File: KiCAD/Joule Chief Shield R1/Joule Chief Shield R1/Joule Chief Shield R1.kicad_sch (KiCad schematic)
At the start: 98 parts, among them J1 Power, J12 Conn_01x06, J13 Conn_01x06, J14 Conn_01x06, J15 Conn_01x06, J16 Conn_01x06, J17 Conn_01x06, J18 Conn_01x06, J2 Digital/PWM, J3 Analog, J4 Digital/PWM, Q10 AO3400A, Q11 AO3400A, Q12 AO3400A, Q3 AO3400A, Q4 AO3400A, Q5 AO3400A, Q6 AO3400A, Q7 AO3400A, Q8 AO3400A, Q9 AO3400A, U11 INA219AxD, U7 LTC3105xMS, U8 AD5280, U9 INA219AxD

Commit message: both schematics finished
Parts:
- removed LITH2: 18650, Joule Thief-Library:18650_Cell_Clip, symbol Device:Battery_Cell
- removed Q3: AO3400A, Package_TO_SOT_SMD:SOT-23, symbol Transistor_FET:AO3400A
- removed R27, R29, R31, R33, R35, R37, R39, R41: 500, Resistor_SMD:R_0805_2012Metric_Pad1.20x1.40mm_HandSolder, symbol Device:R_Small
- removed U10: ~, symbol Joule_Thief_R1:BMS_BOARD
- added C12, C13: 0.1u, Capacitor_SMD:C_0805_2012Metric_Pad1.18x1.45mm_HandSolder, symbol Device:C_Small
- added C14: 10u, Capacitor_SMD:C_0805_2012Metric_Pad1.18x1.45mm_HandSolder, symbol Device:C_Small
- added D1, D2: LED, symbol Device:LED
- added LITH1: 18650, Joule Thief-Library:18650_Cell_Clip, symbol Device:Battery_Cell
- added Q1: AO3400A, Package_TO_SOT_SMD:SOT-23, symbol Transistor_FET:AO3400A
- added R10, R11, R12, R13: 1k, Resistor_SMD:R_0805_2012Metric_Pad1.20x1.40mm_HandSolder, symbol Device:R_Small
- added R14: 10k, Resistor_SMD:R_0805_2012Metric_Pad1.20x1.40mm_HandSolder, symbol Device:R_Small
- added R18, R20, R21, R22, R23, R24, R25: 1K, Resistor_SMD:R_0805_2012Metric_Pad1.20x1.40mm_HandSolder, symbol Device:R_Small
- added R9: 100, Resistor_SMD:R_0805_2012Metric_Pad1.20x1.40mm_HandSolder, symbol Device:R_Small
- added U5: DW01, Package_TO_SOT_SMD:SOT-23-6_Handsoldering, symbol 000_Dropbin:DW01
- added U6: TP4056, Package_SO:SOIC-8-1EP_3.9x4.9mm_P1.27mm_EP2.29x3mm, symbol 000_Dropbin:TP4056
- added U7: FS8205A, Package_TO_SOT_SMD:SOT-23-6_Handsoldering, symbol 000_Dropbin:FS8205A
- R17: renamed from R26; value 500 -> 1K
- R19: value 10k -> 1K
- renumbered C21 to C1, C19 to C10, C18 to C11, C22 to C2, C23 to C3, C17 to C4, C20 to C5, C13 to C6, C14 to C7, C16 to C8, C15 to C9, D8 to D10, D9 to D11, D1 to D3, D2 to D4, D3 to D5, D4 to D6, D5 to D7, D6 to D8, D7 to D9, J12 to J1, J3 to J10, J4 to J11, J13 to J2, J14 to J3, J15 to J4, J16 to J5, J17 to J6, J18 to J7, J2 to J8, J1 to J9, JP41 to JP1, JP30 to JP10, JP31 to JP11, JP32 to JP12, JP40 to JP13, JP39 to JP14, JP38 to JP15, JP37 to JP16, JP36 to JP17, JP35 to JP18, JP34 to JP19, JP42 to JP2, JP33 to JP20, JP43 to JP3, JP44 to JP4, JP45 to JP5, JP46 to JP6, JP47 to JP7, JP48 to JP8, JP29 to JP9, L2 to L1, Q12 to Q10, Q4 to Q2, Q5 to Q3, Q6 to Q4, Q7 to Q5, Q8 to Q6, Q9 to Q7, Q10 to Q8, Q11 to Q9, R21 to R1, R23 to R15, R24 to R16, R20 to R2, R25 to R26, R28 to R27, R30 to R28, R32 to R29, R22 to R3, R34 to R30, R36 to R31, R38 to R32, R40 to R33, R42 to R34, R14 to R4, R15 to R5, R17 to R6, R18 to R7, R16 to R8, U11 to U1, U7 to U2, U8 to U3, U9 to U4
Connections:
- net +5V: now also R19.2, R18.2, R20.2, R21.2, R22.2, R23.2, R24.2, R25.2
- net CHARGER: now also Q1.1 (G), R14.2; no longer R19.2
- net GND: now also Q1.2 (S), R14.1; no longer R19.1
- net at D11.2 (A): now also R25.1
- net at D9.2 (A): now also R23.1
- net at D4.2 (A): now also R18.1
- net at D5.2 (A): now also R19.1
- net at R6.1: now also C13.2, D1.2 (A), D2.2 (A), U6.4 (VCC), U6.8 (CE)
- net at D7.2 (A): now also R21.1
- net at D6.2 (A): now also R20.1
- net at D10.2 (A): now also R24.1
- net at D8.2 (A): now also R22.1
- new net: C13.1, C14.1, Q1.3 (D), R12.1, R13.1, U6.1 (TEMP), U6.3 (GND), U7.6 (S2), U7.7 (S2)
- new net: C12.2, C14.2, R9.1, U5.5 (VCC), U6.5 (BAT)
- new net: U5.1 (OD), U7.4 (G1)
- new net: R12.2, U5.2 (CS)
- new net: U5.3 (OC), U7.5 (G2)
- new net: R13.2, U6.2 (PROG)
- new net: D2.1 (K), R11.1
- new net: D1.1 (K), R10.1
- new net: R10.2, U6.7 (~{CHRG})
- new net: R11.2, U6.6 (~{STDBY})
- new net BAT+: LITH1.1 (+), R9.2
- new net BAT-: C12.1, LITH1.2 (-), U5.6 (GND), U7.2 (S1), U7.3 (S1)
- no-connect marks 5 -> 8
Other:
- note added: "18650 BMS+CHARGING MODULE"
- note removed: "GENERIC BMS MODULE"
- moved on the sheet: C1, C10, C11, C2, C3, C4, C5, C6, C7, C8, C9, D10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

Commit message: ERC+prep for board layout
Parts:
- C2, C5: footprint (none) -> 000_Dropbin:1F_Supercap
- C4: footprint (none) -> Capacitor_THT:CP_Radial_D5.0mm_P2.00mm
- D1, D10, D11, D2, D3, D4, D5, D6, D7, D8, D9: footprint (none) -> LED_SMD:LED_0805_2012Metric_Pad1.15x1.40mm_HandSolder
- J1, J2, J3, J4, J5, J6, J7: footprint (none) -> Connector_JST:JST_PH_B7B-PH-K_1x07_P2.00mm_Vertical
- JP1, JP10, JP11, JP12, JP13, JP14, JP15, JP16, JP17, JP18, JP19, JP2, JP20, JP3, JP4, JP5, JP6, JP7, JP8, JP9: footprint (none) -> Jumper:SolderJumper-2_P1.3mm_Open_RoundedPad1.0x1.5mm
- L1: footprint Joule Thief-Library:Power_Inductor_101040 -> 000_Dropbin:Power_Inductor_101040
- LITH1: footprint Joule Thief-Library:18650_Cell_Clip -> 000_Dropbin:18650_Cell_Clip_V2
- TPx1: footprint (none) -> TestPoint:TestPoint_THTPad_1.0x1.0mm_Drill0.5mm
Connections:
- no-connect marks 8 -> 23
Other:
- note added: "INCOMING POWER MONITOR"
- note added: "OUTGOING POWER MONITOR"
- note removed: "LOAD CELL POWER MONITOR"
- note removed: "SUPPLY CELL POWER MONITOR"

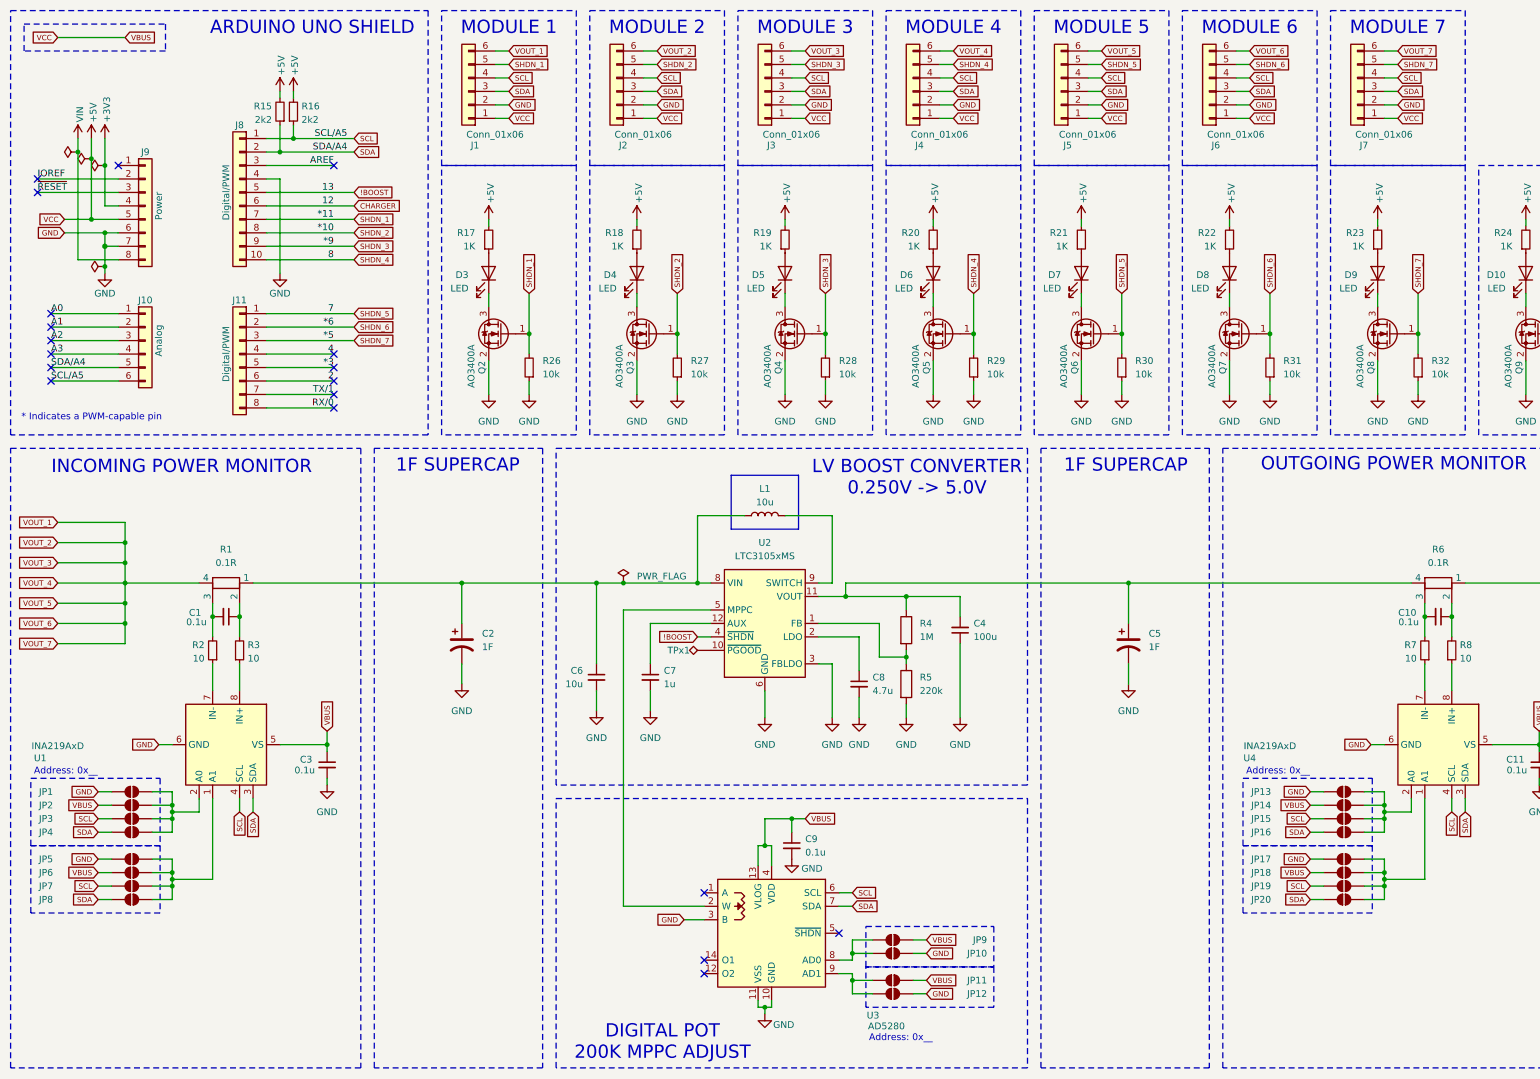
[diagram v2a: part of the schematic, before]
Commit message: layout extraction module
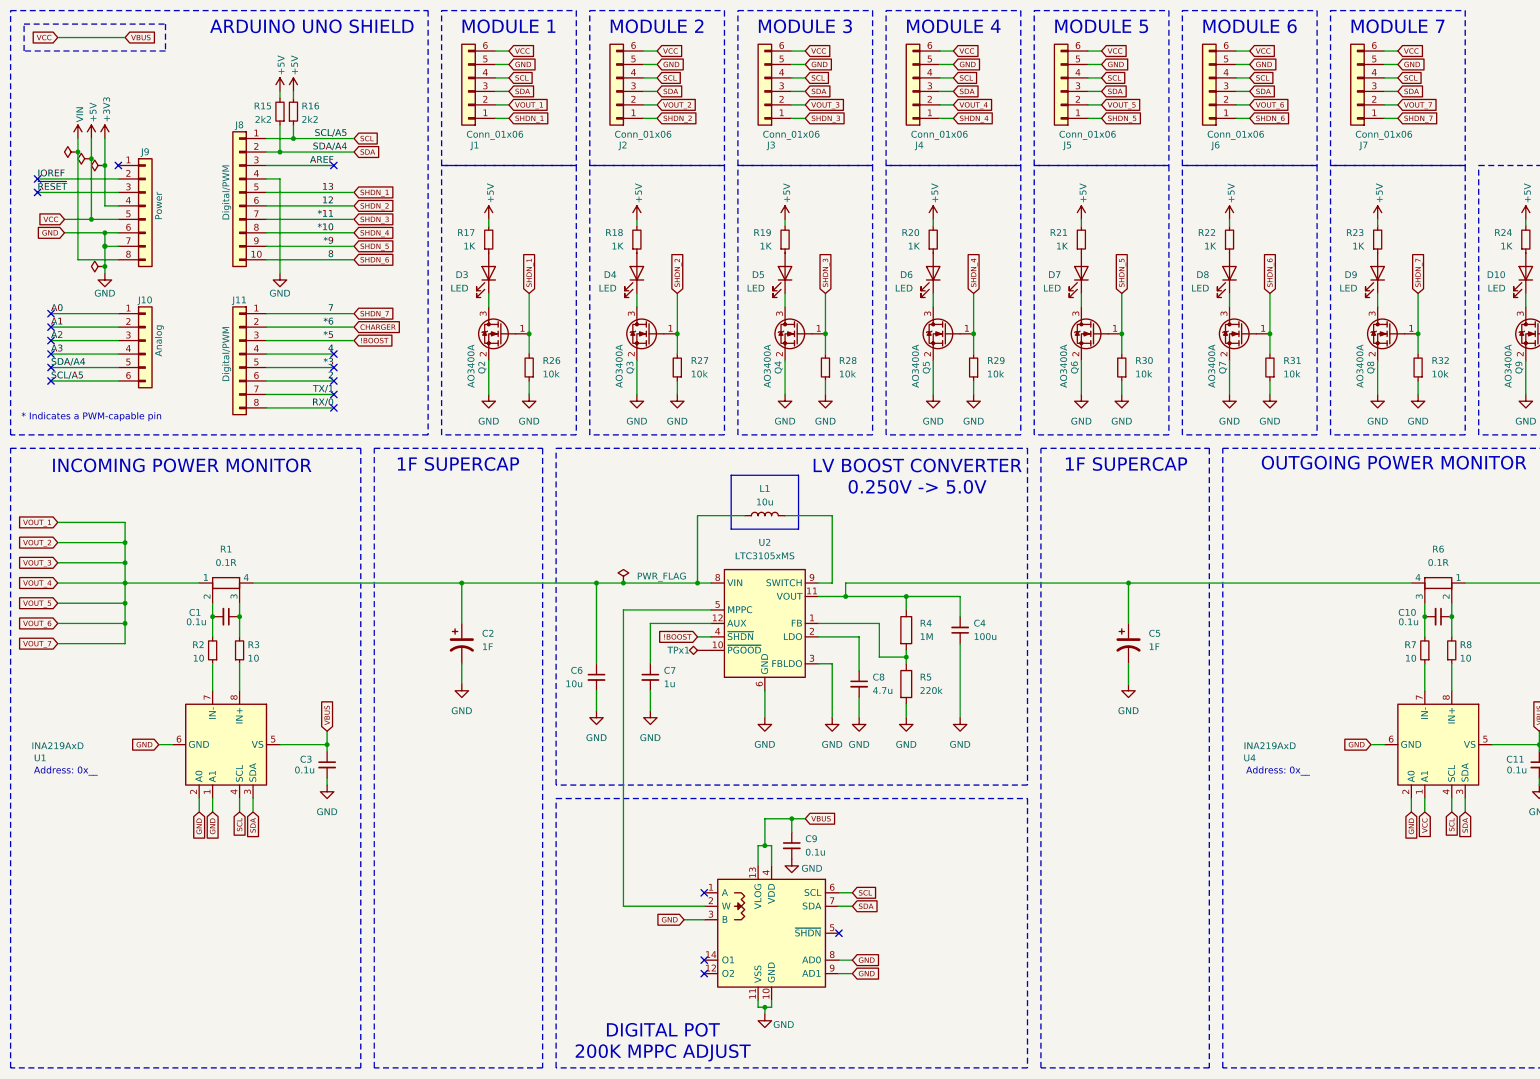
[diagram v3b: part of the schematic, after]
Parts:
- removed JP1, JP10, JP11, JP12, JP13, JP14, JP15, JP16, JP17, JP18, JP19, JP2, JP20, JP3, JP4, JP5, JP6, JP7, JP8, JP9: SolderJumper_2_Open, Jumper:SolderJumper-2_P1.3mm_Open_RoundedPad1.0x1.5mm, symbol Jumper:SolderJumper_2_Open
- J1, J2, J3, J4, J5, J6, J7: footprint Connector_JST:JST_PH_B7B-PH-K_1x07_P2.00mm_Vertical -> Connector_JST:JST_PH_B6B-PH-K_1x06_P2.00mm_Vertical
- R1, R6: footprint Resistor_SMD:R_Shunt_Vishay_WSK2512_6332Metric_T1.19mm -> 000_Dropbin:R_Shunt_2512_V2
- U7: footprint Package_TO_SOT_SMD:SOT-23-6_Handsoldering -> Package_TO_SOT_SMD:SOT-23-8_Handsoldering
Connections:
- net !BOOST: now also J11.3 (Pin_3); no longer J8.5 (Pin_5)
- net +5V: now also J1.6 (Pin_6), J2.6 (Pin_6), J3.6 (Pin_6), J4.6 (Pin_6), J5.6 (Pin_6), J6.6 (Pin_6), J7.6 (Pin_6), U4.1 (A1); no longer J1.1 (Pin_1), J2.1 (Pin_1), J3.1 (Pin_1), J4.1 (Pin_1), J5.1 (Pin_1), J6.1 (Pin_1), J7.1 (Pin_1)
- net CHARGER: now also J11.2 (Pin_2); no longer J8.6 (Pin_6)
- net GND: now also J1.5 (Pin_5), J2.5 (Pin_5), J3.5 (Pin_5), J4.5 (Pin_5), J5.5 (Pin_5), J6.5 (Pin_5), J7.5 (Pin_5), U1.1 (A1), U1.2 (A0), U3.8 (AD0), U3.9 (AD1), U4.2 (A0); no longer J1.2 (Pin_2), J2.2 (Pin_2), J3.2 (Pin_2), J4.2 (Pin_2), J5.2 (Pin_2), J6.2 (Pin_2), J7.2 (Pin_2)
- net SHDN_1: now also J1.1 (Pin_1), J8.5 (Pin_5); no longer J1.5 (Pin_5), J8.7 (Pin_7)
- net SHDN_2: now also J2.1 (Pin_1), J8.6 (Pin_6); no longer J2.5 (Pin_5), J8.8 (Pin_8)
- net SHDN_3: now also J3.1 (Pin_1), J8.7 (Pin_7); no longer J3.5 (Pin_5), J8.9 (Pin_9)
- net SHDN_4: now also J4.1 (Pin_1), J8.8 (Pin_8); no longer J4.5 (Pin_5), J8.10 (Pin_10)
- net SHDN_5: now also J5.1 (Pin_1), J8.9 (Pin_9); no longer J11.1 (Pin_1), J5.5 (Pin_5)
- net SHDN_6: now also J6.1 (Pin_1), J8.10 (Pin_10); no longer J11.2 (Pin_2), J6.5 (Pin_5)
- net SHDN_7: now also J11.1 (Pin_1), J7.1 (Pin_1); no longer J11.3 (Pin_3), J7.5 (Pin_5)
- net VOUT_1: now also J1.2 (Pin_2), J2.2 (Pin_2), J3.2 (Pin_2), J4.2 (Pin_2), J5.2 (Pin_2), J6.2 (Pin_2), J7.2 (Pin_2), R1.1; no longer J1.6 (Pin_6), J2.6 (Pin_6), J3.6 (Pin_6), J4.6 (Pin_6), J5.6 (Pin_6), J6.6 (Pin_6), J7.6 (Pin_6), R1.4
- net at C1.2, R2.2: now also R1.2; no longer R1.3
- net at C2.1, C6.1, L1.1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: now also R1.4; no longer R1.1
- net at C1.1, R3.2: now also R1.3; no longer R1.2
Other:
- moved on the sheet: R1
